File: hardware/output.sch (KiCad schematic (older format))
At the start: 98 parts, among them J79 Conn_01x03, J80 Conn_01x03, J81 Conn_01x03, J82 Screw_Terminal_01x04, J83 Conn_01x03, J84 Conn_01x03, J85 Conn_01x03, J86 Conn_01x03, J87 Conn_01x03, J88 Screw_Terminal_01x02, Q10 AO3400, Q11 AON6144, Q12 AO3400, Q13 AO3400, Q14 AO3400, Q3 AO3400, Q4 AO3400, Q5 AO3400, Q6 AON6144, Q7 AON6144, Q8 AO3400, Q9 AO3400, U7 IR4427S, U8 IR4427S

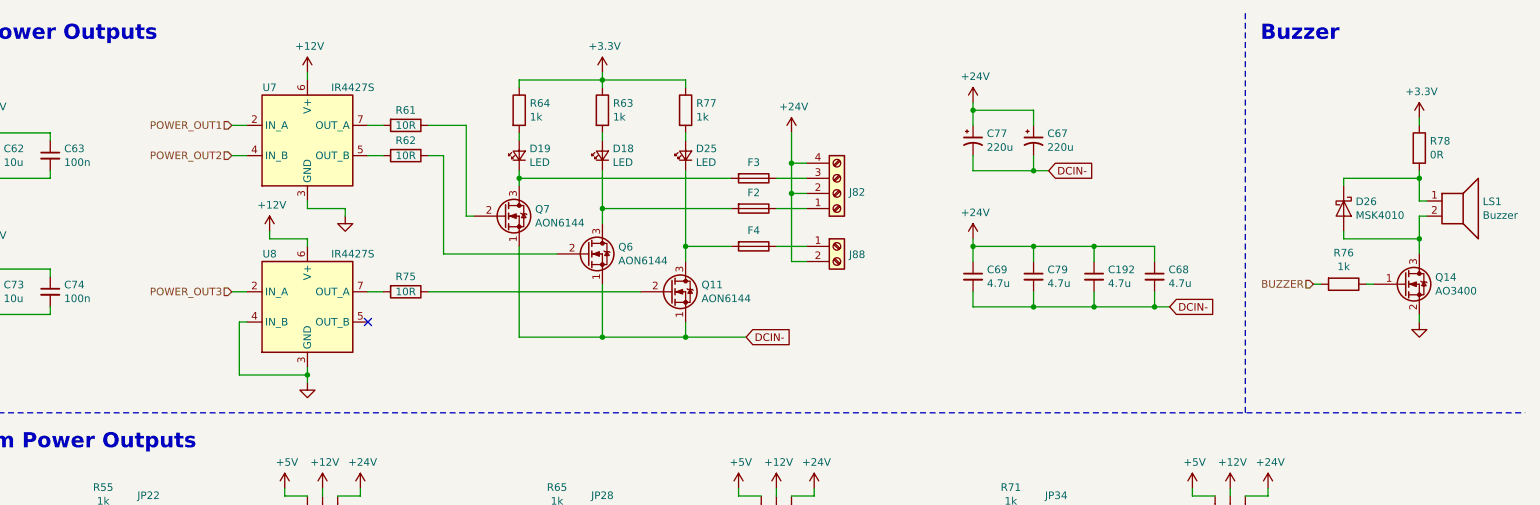
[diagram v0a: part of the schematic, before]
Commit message: replaced stepper driver
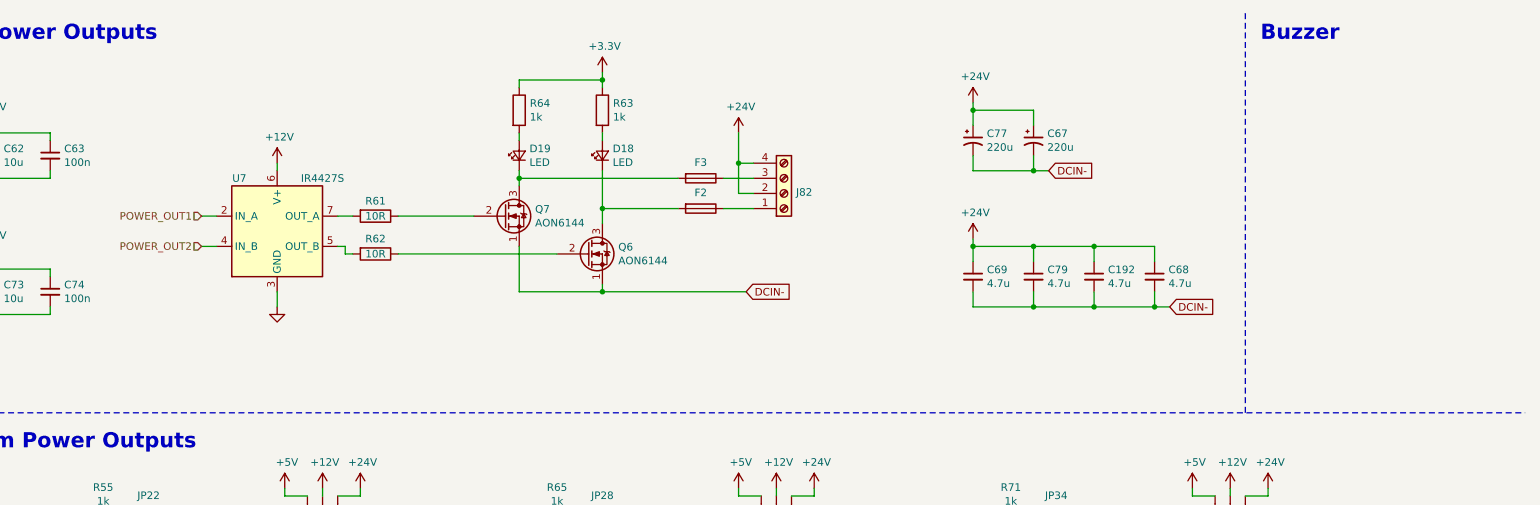
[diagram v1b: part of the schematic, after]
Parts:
- removed D25: LED, _Generic:0603_LED, symbol Device:LED_Small
- removed D26: MSK4010, _Generic:SOD-523_DIODE, symbol Device:D_Schottky
- removed F4: Fuse, _Generic:SMD_Fuseholder, symbol Device:Fuse
- removed J88: Screw_Terminal_01x02, _Generic:KF635-2P, symbol Connector:Screw_Terminal_01x02
- removed LS1: Buzzer, _Generic:Buzzer-7525, symbol Device:Speaker
- removed Q11: AON6144, _Generic:DFN5x6-8, symbol Device:Q_NMOS_SGD
- removed Q14: AO3400, _Generic:SOT-23, symbol Device:Q_NMOS_GSD
- removed R75: 10R, _Generic:0603_RES, symbol Device:R
- removed R76, R77: 1k, _Generic:0603_RES, symbol Device:R
- removed R78: 0R, _Generic:0603_RES, symbol Device:R
- removed U8: IR4427S, _Generic:SO-8, symbol Driver_FET:MIC4427
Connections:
- no-connect marks 1 -> 0
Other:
- moved on the sheet: F2, F3, J82, R61, R62, U7

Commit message: layout
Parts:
- added C? (x2): 4.7u, _Generic:1210_CAP, symbol Device:C_Small
- F2, F3: footprint _Generic:SMD_Fuseholder -> _Generic:1206_RES
- Q6, Q7: value AON6144 -> AON7418; footprint _Generic:DFN5x6-8 -> _Generic:DFN3x3A_8L_EP1_P
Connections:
- net +24V: now also F2.2, F3.2; no longer C192.1, C68.1, C69.1, C79.1, J82.2 (Pin_2), J82.4 (Pin_4)
- net DCIN-: now also C?.2, C?.2
- net at F2.1: now also C69.1, C79.1, J82.2 (Pin_2), C?.1; no longer J82.1 (Pin_1)
- net at D18.1 (K), Q6.3 (D): now also J82.1 (Pin_1); no longer F2.2
- net at F3.1: now also C192.1, C68.1, J82.4 (Pin_4), C?.1; no longer J82.3 (Pin_3)
- net at D19.1 (K), Q7.3 (D): now also J82.3 (Pin_3); no longer F3.2
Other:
- note removed: "Buzzer"
- moved on the sheet: C192, C67, C68, C69, C77, C79, F2, F3, J82

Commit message: power reg
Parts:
- removed C73: 10u, _Generic:0603_CAP, symbol Device:C_Small
- removed C74: 100n, _Generic:0603_CAP, symbol Device:C_Small
- gave numbers to parts that had none: 2
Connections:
- net +3V3 is gone; now on net +12V: R63.1, R64.1
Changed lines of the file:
@@
 	4500 1350 4500 1400
-$Comp
-L power:+3.3V #PWR087
-U 1 1 60710092
-P 5050 950
-F 0 "#PWR087" H 5050 800 50  0001 C CNN
-F 1 "+3.3V" H 5065 1123 50  0000 C CNN
-F 2 "" H 5050 950 50  0001 C CNN
-F 3 "" H 5050 950 50  0001 C CNN
-	1    5050 950
-	1    0    0    -1
-$EndComp
 $Comp
 L Device:R R63
@@
 	9200 4000 9200 3950
 $Comp
-L Device:C_Small C74
-U 1 1 5CEA846E
-P 1400 2400
-F 0 "C74" H 1492 2446 50  0000 L CNN
-F 1 "100n" H 1492 2355 50  0000 L CNN
-F 2 "_Generic:0603_CAP" H 1400 2400 50  0001 C CNN
-F 3 "~" H 1400 2400 50  0001 C CNN
-	1    1400 2400
-	1    0    0    -1
-$EndComp
-$Comp
-L Device:C_Small C73
-U 1 1 5CEA8475
-P 1000 2400
-F 0 "C73" H 1092 2446 50  0000 L CNN
-F 1 "10u" H 1092 2355 50  0000 L CNN
-F 2 "_Generic:0603_CAP" H 1000 2400 50  0001 C CNN
-F 3 "~" H 1000 2400 50  0001 C CNN
-	1    1000 2400
-	1    0    0    -1
-$EndComp
-Wire Wire Line
-	1000 2300 1000 2250
-Wire Wire Line
-	1000 2250 1400 2250
-Wire Wire Line
-	1400 2250 1400 2300
-Wire Wire Line
-	1000 2550 1000 2500
-Wire Wire Line
-	1400 2550 1400 2500
-Wire Wire Line
-	1000 2550 1400 2550
-$Comp
 L Device:C_Small C79
 U 1 1 5CEA84EA
@@
 Wire Wire Line
 	5650 1350 5650 1550
-$Comp
-L #Power:GND #PWR?
-U 1 1 5F12D369
-P 1000 2600
-AR Path="/5AF7E834/5F12D369" Ref="#PWR?"  Part="1"
-AR Path="/5AF7E834/606BF39C/5F12D369" Ref="#PWR?"  Part="1"
-AR Path="/606BF39C/5F12D369" Ref="#PWR0120"  Part="1"
-F 0 "#PWR0120" H 1000 2350 50  0001 C CNN
-F 1 "GND" H 1000 2450 50  0001 C CNN
-F 2 "" H 1000 2600 50  0001 C CNN
-F 3 "" H 1000 2600 50  0001 C CNN
-	1    1000 2600
-	1    0    0    -1
-$EndComp
-Wire Wire Line
-	1000 2550 1000 2600
-Connection ~ 1000 2550
-$Comp
-L power:+12V #PWR0122
-U 1 1 5F1D3595
-P 1000 2200
-F 0 "#PWR0122" H 1000 2050 50  0001 C CNN
-F 1 "+12V" H 1015 2373 50  0000 C CNN
-F 2 "" H 1000 2200 50  0001 C CNN
-F 3 "" H 1000 2200 50  0001 C CNN
-	1    1000 2200
-	1    0    0    -1
-$EndComp
-Wire Wire Line
-	1000 2200 1000 2250
-Connection ~ 1000 2250
 $Comp
 L power:+12V #PWR0202
@@
 	6000 1550 7550 1550
 $Comp
-L Device:C_Small C?
+L Device:C_Small C73
 U 1 1 5D51CEB0
 P 6900 2200
-F 0 "C?" H 6992 2246 50  0000 L CNN
+F 0 "C73" H 6992 2246 50  0000 L CNN
 F 1 "4.7u" H 6992 2155 50  0000 L CNN
 F 2 "_Generic:1210_CAP" H 6900 2200 50  0001 C CNN
@@
 	7550 2300 7550 2400
 $Comp
-L Device:C_Small C?
+L Device:C_Small C74
 U 1 1 5D53DF87
 P 7550 2200
-F 0 "C?" H 7642 2246 50  0000 L CNN
+F 0 "C74" H 7642 2246 50  0000 L CNN
 F 1 "4.7u" H 7642 2155 50  0000 L CNN
 F 2 "_Generic:1210_CAP" H 7550 2200 50  0001 C CNN
@@
 Wire Wire Line
 	7550 1550 7950 1550
+$Comp
+L power:+12V #PWR0120
+U 1 1 5D200D5D
+P 5050 950
+F 0 "#PWR0120" H 5050 800 50  0001 C CNN
+F 1 "+12V" H 5065 1123 50  0000 C CNN
+F 2 "" H 5050 950 50  0001 C CNN
+F 3 "" H 5050 950 50  0001 C CNN
+	1    5050 950
+	1    0    0    -1
+$EndComp
 $EndSCHEMATC

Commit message: layout
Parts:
- removed JP22, JP23, JP24, JP28, JP29, JP30, JP34, JP35: SolderJumper_3_Open, _Generic:Solder Jumper 3P, symbol #PCB_Only:SolderJumper_3_Open
- added JP10, JP11, JP12, JP13, JP14, JP2, JP22, JP23, JP24, JP3, JP4, JP5, JP6, JP7, JP8, JP9: SolderJumper_2_Open, _Generic:Solder Jumper 2P, symbol #PCB_Only:SolderJumper_2_Open
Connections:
- net +24V: now also JP25.2 (O1), JP27.2 (O1), JP32.2 (O1), JP37.2 (O1); no longer JP25.4 (O4), JP27.4 (O4), JP32.4 (O4), JP37.4 (O4)
- net +5V: now also JP25.4 (O4), JP27.4 (O4), JP32.4 (O4), JP37.4 (O4); no longer JP25.2 (O1), JP27.2 (O1), JP32.2 (O1), JP37.2 (O1)
- net at R65.2: now also JP11.1 (A), JP8.1 (A)
- net at J83.3 (Pin_3), Q8.3 (D): now also JP11.2 (B)
- net at Q8.1 (G), R66.2: now also JP8.2 (B)
- net at R67.2: now also JP12.1 (A), JP9.1 (A)
- net at J84.3 (Pin_3), Q9.3 (D): now also JP12.2 (B)
- net at Q9.1 (G), R68.2: now also JP9.2 (B)
- net at R69.2: now also JP10.1 (A), JP13.1 (A)
- net at J85.3 (Pin_3), Q10.3 (D): now also JP13.2 (B)
- net at Q10.1 (G), R70.2: now also JP10.2 (B)
- net at R57.2: now also JP3.1 (A), JP6.1 (A)
- net at J80.3 (Pin_3), Q4.3 (D): now also JP6.2 (B)
- net at Q4.1 (G), R58.2: now also JP3.2 (B)
- net at R59.2: now also JP4.1 (A), JP7.1 (A)
- net at J81.3 (Pin_3), Q5.3 (D): now also JP7.2 (B)
- net at Q5.1 (G), R60.2: now also JP4.2 (B)
- net at R73.2: now also JP22.1 (A), JP24.1 (A)
- net at J87.3 (Pin_3), Q13.3 (D): now also JP24.2 (B)
- net at Q13.1 (G), R74.2: now also JP22.2 (B)
- net at R71.2: now also JP14.1 (A), JP23.1 (A)
- net at J86.3 (Pin_3), Q12.3 (D): now also JP23.2 (B)
- net at Q12.1 (G), R72.2: now also JP14.2 (B)
- net at R55.2: now also JP2.1 (A), JP5.1 (A)
- net at J79.3 (Pin_3), Q3.3 (D): now also JP5.2 (B)
- net at Q3.1 (G), R56.2: now also JP2.2 (B)

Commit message: combine
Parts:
- removed C192, C68, C69, C73, C74, C79: 4.7u, _Generic:1210_CAP, symbol Device:C_Small
- removed C62: 10u, _Generic:0603_CAP, symbol Device:C_Small
- removed C63: 100n, _Generic:0603_CAP, symbol Device:C_Small
- removed C67, C77: 220u, Capacitor_SMD:CP_Elec_6.3x7.7, symbol Device:CP1_Small
- removed D15: 3.6v, _Generic:SOD-523_DIODE, symbol Device:D_Zener
- removed D18, D19: LED, _Generic:0603_LED, symbol Device:LED_Small
- removed F2, F3: Fuse, _Generic:1206_RES, symbol Device:Fuse
- removed J82: Screw_Terminal_01x04, _Generic:KF635-4P, symbol Connector:Screw_Terminal_01x04
- removed Q6, Q7: AON7418, _Generic:DFN3x3A_8L_EP1_P, symbol Device:Q_NMOS_SGD
- removed R61, R62: 10R, _Generic:0603_RES, symbol Device:R
- removed R63, R64: 1k, _Generic:0603_RES, symbol Device:R
- removed U7: IR4427S, _Generic:SO-8, symbol Driver_FET:MIC4427
- Q3: value AO3400 -> AO3402
- R55: value 1k -> 4.7k
- R56: value 47k -> 1meg
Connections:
- net GND: now also R56.2; no longer R56.1
- net at JP2.1 (A), R55.2: now also JP5.2 (B); no longer JP5.1 (A)
- net at J79.3 (Pin_3), Q3.3 (D): now also JP5.1 (A); no longer JP5.2 (B)
- net at JP2.2 (B), Q3.1 (G): now also R56.1; no longer R56.2
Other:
- note removed: "High Power Outputs"
- moved on the sheet: C64, J79, JP2, JP25, JP5, Q3, R55, R56

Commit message: new con
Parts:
- added D15: 3.6v, _Generic:SOD-523_DIODE, symbol Device:D_Zener
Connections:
- net GND: now also D15.2 (A)
- net HV_IO1: now also JP2.2 (B), Q3.1 (G), R56.1, D15.1 (K)
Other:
- moved on the sheet: JP2, JP25, JP5, R56
